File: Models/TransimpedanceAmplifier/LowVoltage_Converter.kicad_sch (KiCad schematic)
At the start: 4 parts, among them U10 LM78L05, 5V, 5%, U8 TLV76133, 3.3V, 1%

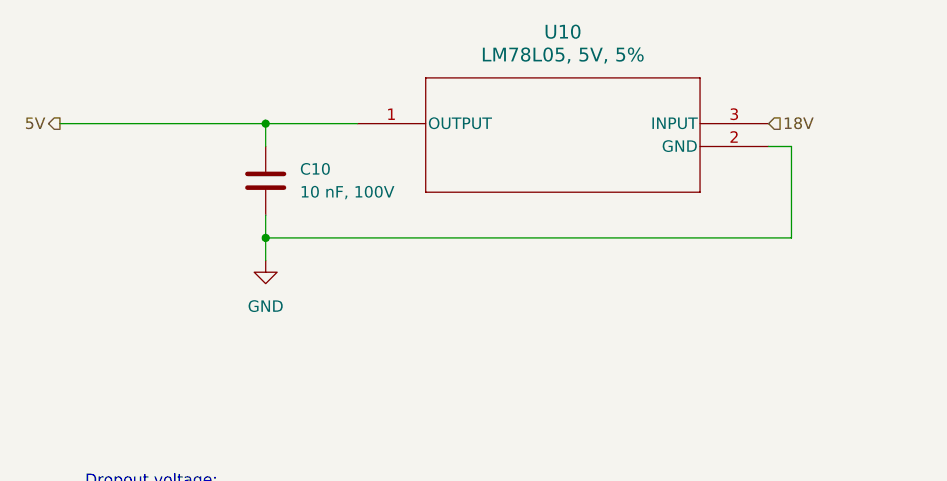
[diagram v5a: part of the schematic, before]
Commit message: Deleted all schematics for voltage regulators
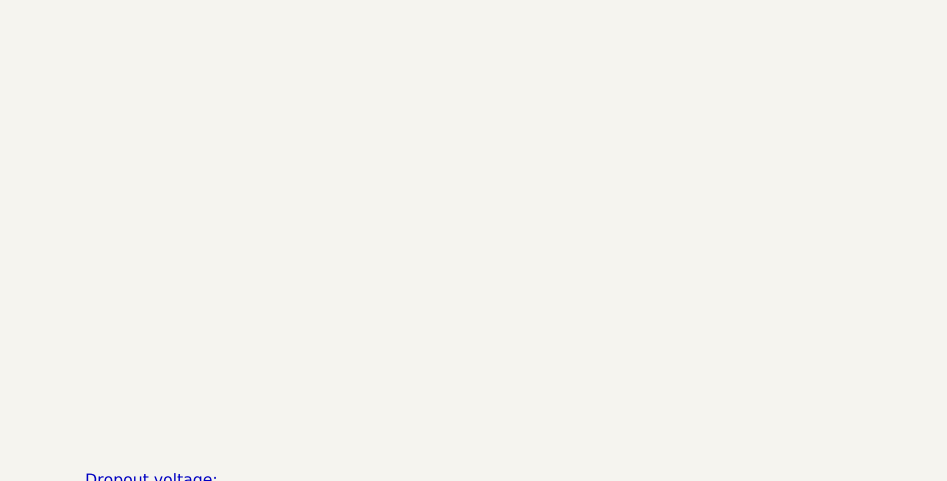
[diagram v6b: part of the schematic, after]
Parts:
- removed C10: 10 nF, 100V, symbol Device:C
- removed U10: LM78L05, 5V, 5%, LP3_TEX, symbol LM78L:LM78L05ACZ_LFT1

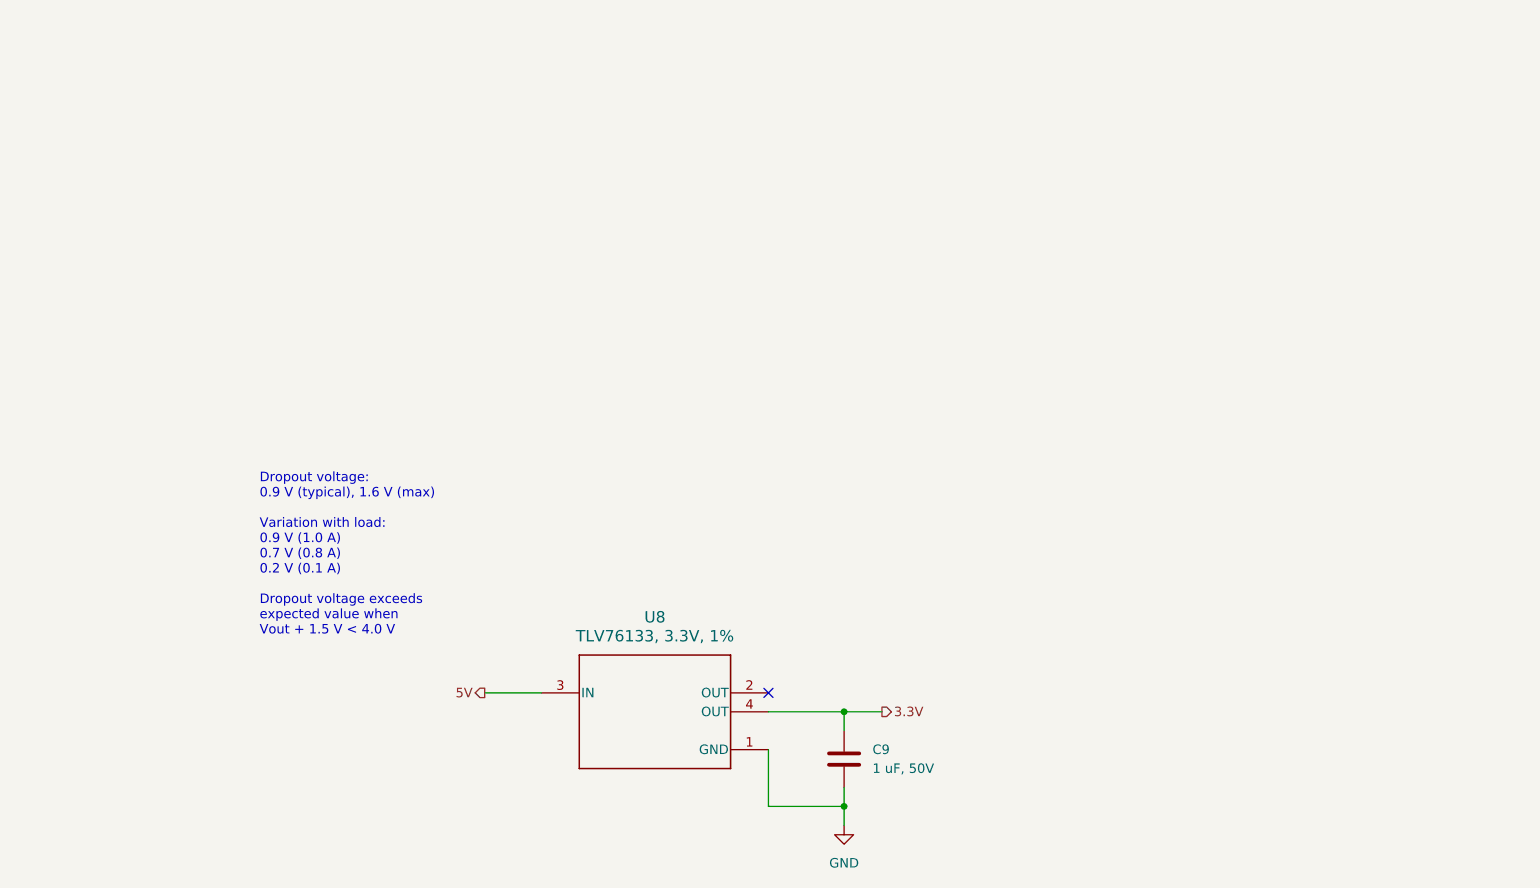
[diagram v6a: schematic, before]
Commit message: Finished rewriting the schematic, just need purchase links for the new regulators
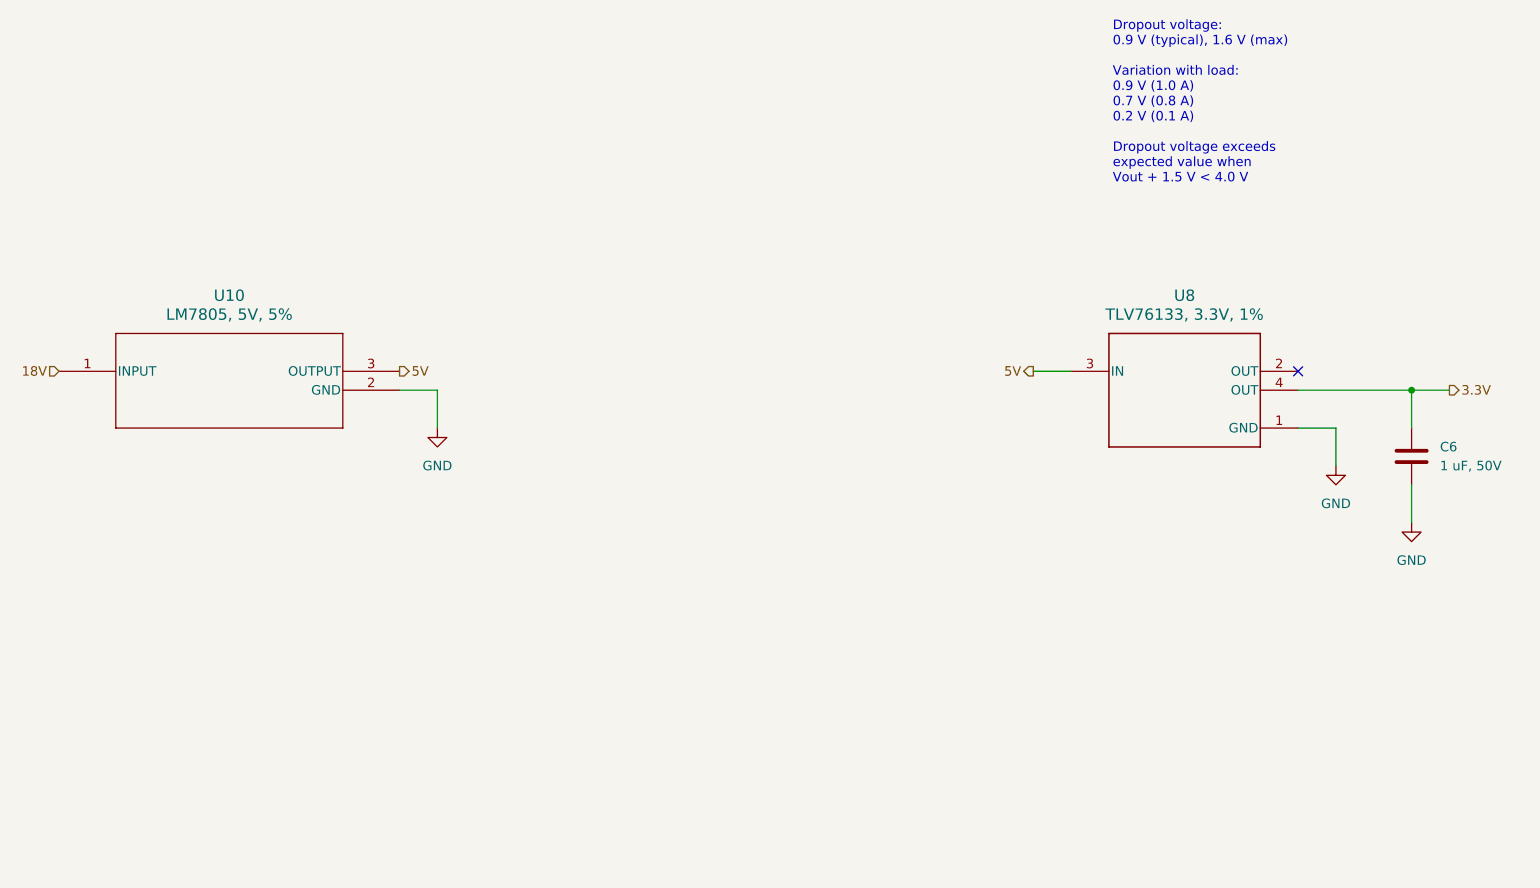
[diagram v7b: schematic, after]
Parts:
- removed C9: 1 uF, 50V, symbol Device:C
- added C6: 1 uF, 50V, symbol Device:C
- added U10: LM7805, 5V, 5%, NDE3_TEX, symbol LM78:LM7805CT_NOPB
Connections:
- net 3.3V: now also C6.1
- net 5V: now also U10.3 (OUTPUT)
- net GND: now also C6.2, U10.2 (GND)
- new net 18V: U10.1 (INPUT)
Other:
- moved on the sheet: U8

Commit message: Overhauled the purchase links for regulators and trimpots
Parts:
- U10: Purchase Link (none) -> https://www.digikey.com/en/products/detail/texas-instrument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
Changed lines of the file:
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@@
+			)
+		)
+		(property "Purchase Link" "https://www.digikey.com/en/products/detail/texas-instruments/LM7805CT-NOPB/3901929"
+			(at 62.23 81.28 0)
+			(effects
+				(font
+					(size 1.27 1.27)
+				)
+				(hide yes)
 			)
 		)
